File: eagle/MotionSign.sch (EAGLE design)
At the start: 77 parts, among them Q1 16MHZ, U1 ATMEGA328, U2 L7805CDT-TR, U3 NCS36000, U4 PIR, U5 WS2801, U6 SPX3819, U7 NJVMJD2955T4G, U8 TXB0108PWR, U9 LCD-16X2NOHOLES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

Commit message: Work on Board
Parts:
- removed BRGT: 1K, resistor:R-TRIMM3296W
- removed D8: 1n4148, microbuilder:DIODESOD-323
- removed S2: (no value), SparkFun-Electromechanical:SWITCH-SPDT-SMD-A
- added MODE: (no value), SparkFun-Connectors:CONN_02
- added R24: 220, resistor:R-US_0204/7
- U9: value LCD-16X2NOHOLES -> LCD-HD4478020X4-4HOLES; device SparkFun-Displays:LCD-16X2NOHOLES -> HD44780LCD:LCD-HD447804-HOLES20X4-4HOLES
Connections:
- removed net A1: BRGT.S, U9.A
- removed net RESET_5V: D8.C
- new net N$25: R24.2, U9.A
- net GND: now also MODE.1; no longer S2.S
- net LCD4_ESP: now also U8.A6, X2.GPIO13; no longer U8.A3, X2.GPIO16
- net LCD5_ESP: now also U8.A5, X2.GPIO12; no longer U8.A4, X2.GPIO14
- net LCD6_ESP: now also U8.A4, X2.GPIO14; no longer U8.A5, X2.GPIO12
- net LCD7_ESP: now also U8.A3, X2.GPIO16; no longer U8.A6, X2.GPIO13
- net LCD_D4: now also U8.B6; no longer U8.B3
- net LCD_D5: now also U8.B5; no longer U8.B4
- net LCD_D6: now also U8.B4; no longer U8.B5
- net LCD_D7: now also U8.B3; no longer U8.B6
- net MODE: now also MODE.2; no longer S2.P
- net RESET_HZA: no longer D8.A
- net VCC: now also R24.1; no longer BRGT.E

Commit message: V0 of board
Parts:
- U9: device HD44780LCD:LCD-HD447804-HOLES20X4-4HOLES -> HD44780LCD:LCD-HD44780
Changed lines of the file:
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@@
 </variantdefs>
 <classes>
-<class number="0" name="default" width="0.254" drill="0.381">
+<class number="0" name="default" width="0.254" drill="0.254">
 <clearance class="0" value="0.254"/>
 </class>
@@
 <part name="S3" library="SparkFun-Switches" deviceset="MOMENTARY-SWITCH-SPST" device="-SMD-5.2-REDUNDANT" value="Reset"/>
 <part name="S4" library="SparkFun-Switches" deviceset="MOMENTARY-SWITCH-SPST" device="-SMD-5.2-REDUNDANT" value="GPIO0"/>
-<part name="U9" library="HD44780LCD" deviceset="LCD-HD44780" device="20X4-4HOLES" technology="4-HOLES" value="LCD-HD4478020X4-4HOLES"/>
+<part name="U9" library="HD44780LCD" deviceset="LCD-HD44780" device="" value="LCD-HD4478020X4-4HOLES"/>
 <part name="GND23" library="supply1" deviceset="GND" device=""/>
 <part name="VCC" library="SparkFun-Aesthetics" deviceset="VCC" device="" value="VCC"/>

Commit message: Fix board issues
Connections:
- removed net E: U8.B2
- net LCD_E: now also U8.B2
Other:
- moved on the sheet: C1
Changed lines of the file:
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@@
 <?xml version="1.0" encoding="utf-8"?>
 <!DOCTYPE eagle SYSTEM "eagle.dtd">
-<eagle version="8.7.1">
+<eagle version="9.0.1">
 <drawing>
 <settings>
@@
 </instance>
 <instance part="GND1" gate="1" x="170.18" y="101.6"/>
-<instance part="C1" gate="G$1" x="165.1" y="142.24" smashed="yes" rot="R180">
+<instance part="C1" gate="G$1" x="165.1" y="139.7" smashed="yes" rot="R180">
 <attribute name="NAME" x="166.116" y="142.367" size="1.778" layer="95"/>
 <attribute name="VALUE" x="166.116" y="137.541" size="1.778" layer="96"/>
@@
 </segment>
 <segment>
-<wire x1="165.1" y1="134.62" x2="165.1" y2="139.7" width="0.1524" layer="91"/>
+<wire x1="165.1" y1="134.62" x2="165.1" y2="137.16" width="0.1524" layer="91"/>
 <pinref part="C1" gate="G$1" pin="1"/>
 <pinref part="GND7" gate="1" pin="GND"/>
@@
 <net name="AREF" class="0">
 <segment>
-<wire x1="182.88" y1="147.32" x2="165.1" y2="147.32" width="0.1524" layer="91"/>
 <label x="172.72" y="147.32" size="1.778" layer="95"/>
 <pinref part="C1" gate="G$1" pin="2"/>
 <pinref part="U1" gate="G$1" pin="AREF"/>
+<wire x1="165.1" y1="144.78" x2="165.1" y2="147.32" width="0.1524" layer="91"/>
+<wire x1="165.1" y1="147.32" x2="182.88" y2="147.32" width="0.1524" layer="91"/>
 </segment>
 </net>
@@
 </segment>
 </net>
-<net name="E" class="0">
-<segment>
-<pinref part="U8" gate="G$1" pin="B2"/>
-<wire x1="116.84" y1="220.98" x2="119.38" y2="220.98" width="0.1524" layer="91"/>
-<label x="119.38" y="220.98" size="1.27" layer="95" xref="yes"/>
-</segment>
-</net>
 <net name="LCD_D4" class="0">
 <segment>
@@
 <label x="71.12" y="302.26" size="1.27" layer="95" rot="R180" xref="yes"/>
 </segment>
-</net>
+<segment>
+<pinref part="U8" gate="G$1" pin="B2"/>
+<wire x1="116.84" y1="220.98" x2="119.38" y2="220.98" width="0.1524" layer="91"/>
+<label x="119.38" y="220.98" size="1.27" layer="95" xref="yes"/>
+</segment>
+</net>

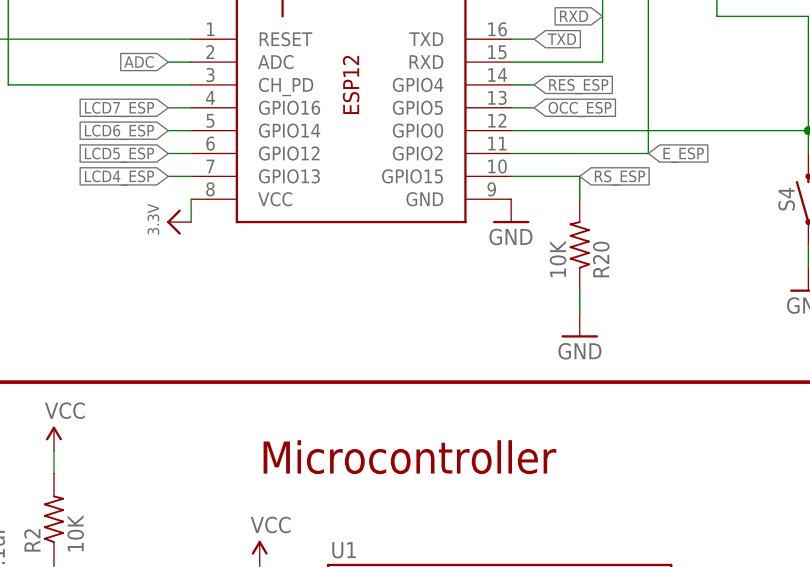
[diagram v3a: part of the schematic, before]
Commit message: Switch GPIO4/GPIO5 pins
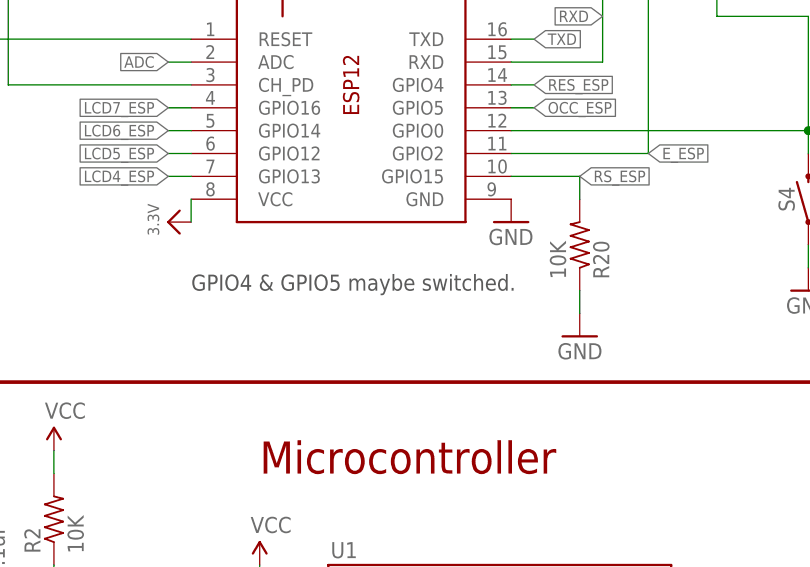
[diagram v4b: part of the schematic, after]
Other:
- note added: "GPIO4 & GPIO5 maybe switched."
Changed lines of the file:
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@@
 <text x="2.54" y="228.6" size="3.556" layer="94" ratio="15">Board LED</text>
 <text x="71.12" y="248.92" size="3.556" layer="94" ratio="15">Level Shifter</text>
+<text x="172.72" y="195.58" size="1.778" layer="97">GPIO4 &amp; GPIO5 maybe switched.</text>
 </plain>
 <instances>

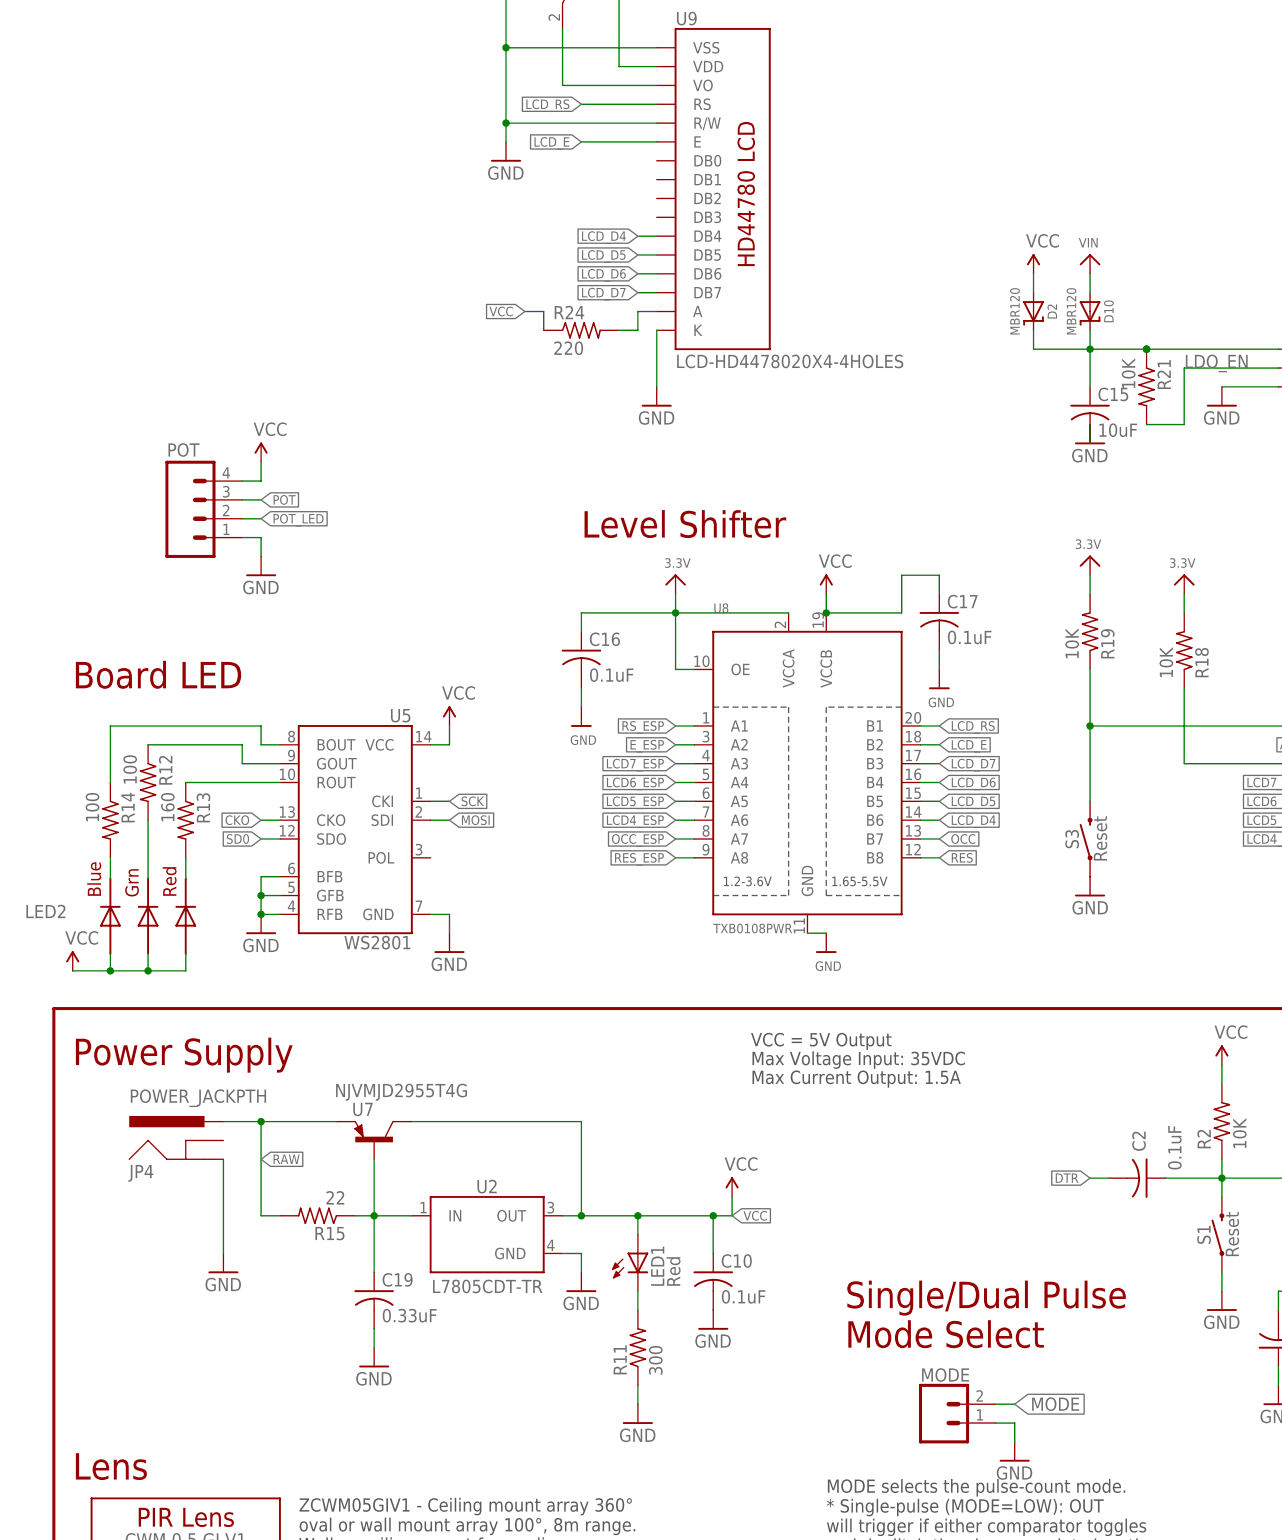
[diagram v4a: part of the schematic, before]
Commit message: Add 5V jumper
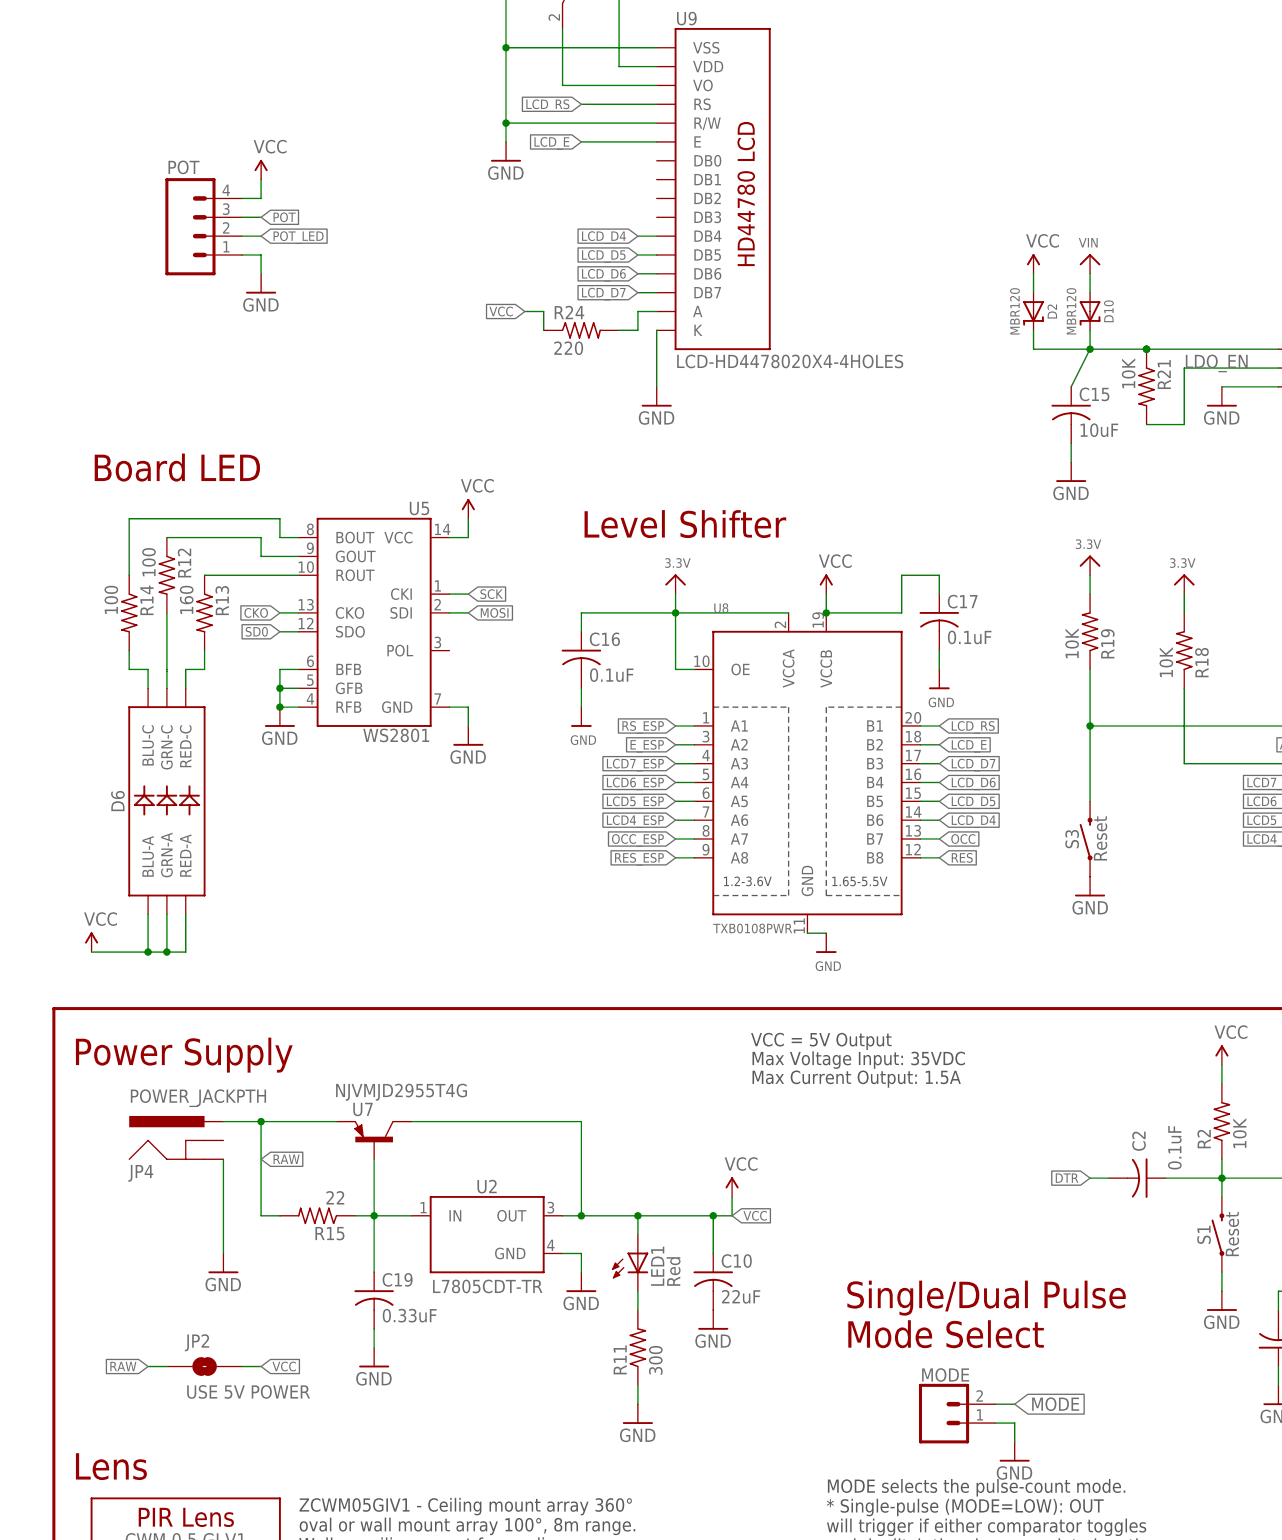
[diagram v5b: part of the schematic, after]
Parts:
- removed LED2: RGBLED5050, adafruit:RGBLED5050
- added D6: (no value), SparkFun-LED:LED-RGBNO_IC
- added JP2: USE 5V POWER, SparkFun-Jumpers:JUMPER-SMT_2_NO_SILK
- C10: value 0.1uF -> 22uF
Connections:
- net N$20: now also D6.BLU-C; no longer LED2.BLUE_C
- net N$21: now also D6.GRN-C; no longer LED2.GREEN_C
- net N$22: now also D6.RED-C; no longer LED2.RED_C
- net RAW: now also JP2.1
- net VCC: now also D6.BLU-A, D6.GRN-A, D6.RED-A, JP2.2; no longer LED2.BLUE_A, LED2.GREEN_A, LED2.RED_A
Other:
- moved on the sheet: C15, POT, R12, R13, R14, U5
